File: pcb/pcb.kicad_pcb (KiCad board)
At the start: 2 copper layers, 136 x 91.9 mm, 56 parts, among them J1 BATT, J2 BATT, SW1 SW_SPST, SW10 SW_SPST, SW11 SW_SPST, SW12 SW_SPST, SW13 SW_SPST, SW14 SW_SPST, SW15 SW_SPST, SW16 SW_SPST, SW17 SW_SPST, SW18 SW_SPST, SW19 SW_SPST, SW2 SW_SPST, SW20 SW_SPST, SW21 SW_SPST, SW3 SW_SPST, SW4 SW_SPST, SW5 SW_SPST, SW6 SW_SPST, SW7 SW_SPST, SW8 SW_SPST, SW9 SW_SPST, U1 XIAO_nRF52840

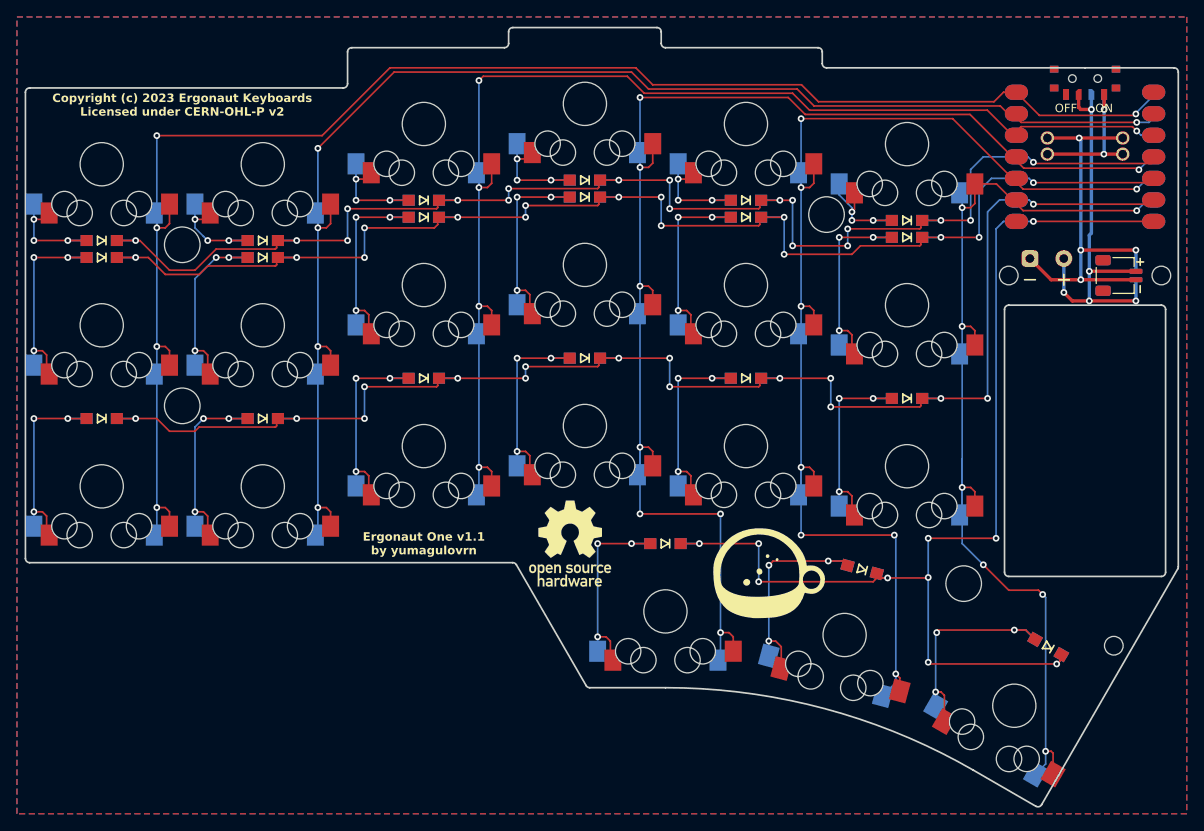
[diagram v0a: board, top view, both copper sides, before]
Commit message: fix: fix outline fillets
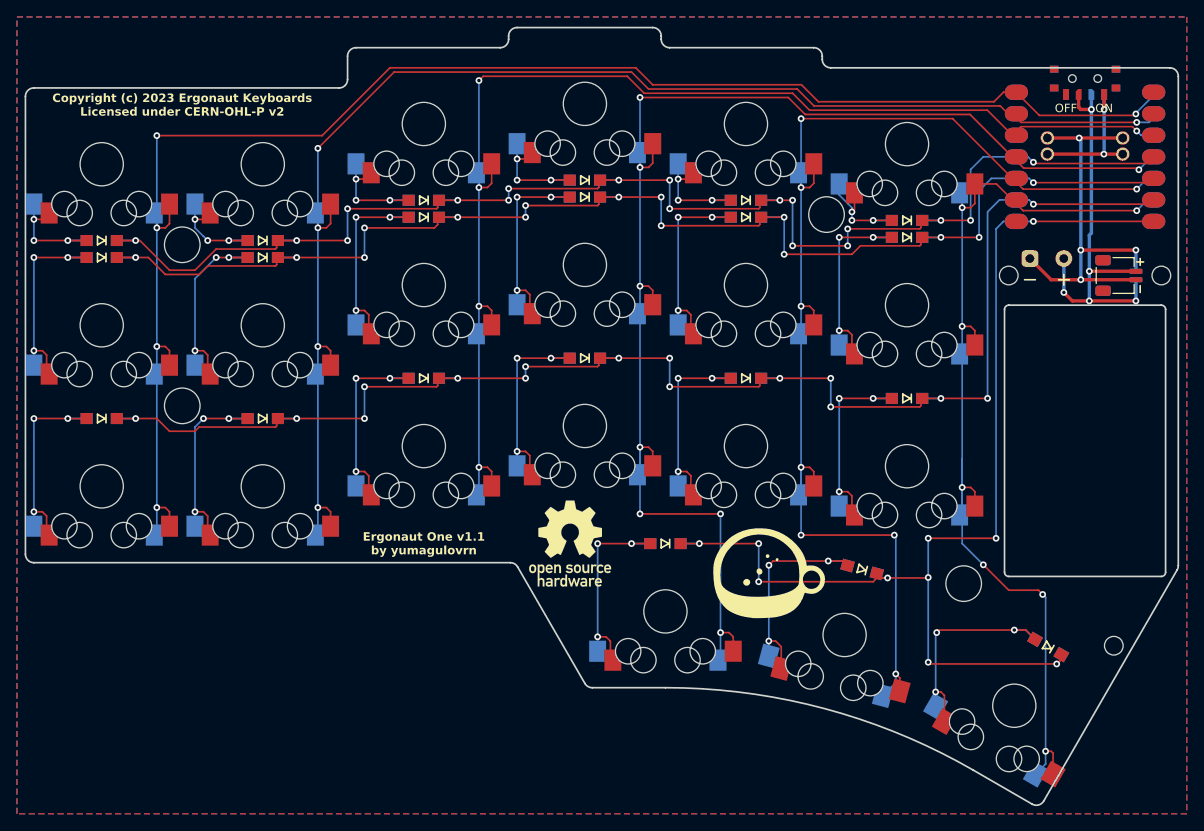
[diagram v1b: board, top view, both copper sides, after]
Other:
- board size 136 x 91.9 mm -> 136 x 91.7 mm
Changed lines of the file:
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@@
     (pad_to_mask_clearance 0)
     (aux_axis_origin 75 0)
-    (grid_origin 196.153537 0)
+    (grid_origin 75 57.49097)
     (pcbplotparams
       (layerselection 0x00010fc_ffffffff)
@@
     )
   )
-  (gr_line (start 75.5 113.49097) (end 75.5 58.49097)
+  (gr_arc (start 113.5 54.240978) (mid 113.79289 53.533866) (end 114.5 53.240978)
     (stroke (width 0.2) (type solid)) (layer "Edge.Cuts"))
-  (gr_arc (start 170 55.61597) (mid 169.646444 55.469524) (end 169.5 55.11597)
+  (gr_arc (start 210.5 55.615978) (mid 211.207104 55.908872) (end 211.5 56.615978)
     (stroke (width 0.2) (type solid)) (layer "Edge.Cuts"))
-  (gr_line (start 170 55.61597) (end 200.5 55.616046)
+  (gr_arc (start 132.695564 113.990978) (mid 133.195576 114.12494) (end 133.56159 114.490978)
     (stroke (width 0.2) (type solid)) (layer "Edge.Cuts"))
-  (gr_arc (start 142.07735 128.7407) (mid 141.827328 128.673735) (end 141.644338 128.4907)
+  (gr_line (start 132.695564 113.990978) (end 76.5 113.990978)
     (stroke (width 0.2) (type solid)) (layer "Edge.Cuts"))
-  (gr_line (start 132.5 52.74097) (end 132.5 51.36597)
+  (gr_arc (start 151 128.740708) (mid 169.805705 131.216526) (end 187.329832 138.475257)
     (stroke (width 0.2) (type solid)) (layer "Edge.Cuts"))
-  (gr_line (start 133 50.86597) (end 150 50.86597)
+  (gr_line (start 210 84.11597) (end 210 115.11597)
     (stroke (width 0.2) (type solid)) (layer "Edge.Cuts"))
-  (gr_line (start 150.5 51.36597) (end 150.5 52.74097)
+  (gr_line (start 191.5 83.61597) (end 209.5 83.61597)
     (stroke (width 0.2) (type solid)) (layer "Edge.Cuts"))
-  (gr_arc (start 211.5 114.477316) (mid 211.482974 114.60673) (end 211.433013 114.727316)
+  (gr_arc (start 132.5 51.865978) (mid 132.79289 51.158866) (end 133.5 50.865978)
     (stroke (width 0.2) (type solid)) (layer "Edge.Cuts"))
-  (gr_line (start 210 84.11597) (end 210 115.11597)
+  (gr_line (start 211.5 56.615978) (end 211.5 114.343349)
     (stroke (width 0.2) (type solid)) (layer "Edge.Cuts"))
-  (gr_line (start 211.5 56.11597) (end 211.5 114.477316)
+  (gr_line (start 151.5 53.240978) (end 168.5 53.240978)
     (stroke (width 0.2) (type solid)) (layer "Edge.Cuts"))
-  (gr_arc (start 151 53.24097) (mid 150.646444 53.094524) (end 150.5 52.74097)
+  (gr_arc (start 195.624061 142.109232) (mid 195.016852 142.575199) (end 194.258035 142.475257)
     (stroke (width 0.2) (type solid)) (layer "Edge.Cuts"))
-  (gr_line (start 191.5 83.61597) (end 209.5 83.61597)
+  (gr_line (start 141.5 128.240708) (end 133.56159 114.490978)
+    (stroke (width 0.2) (type solid)) (layer "Edge.Cuts"))
+  (gr_line (start 194.258035 142.475257) (end 187.329832 138.475257)
+    (stroke (width 0.2) (type solid)) (layer "Edge.Cuts"))
+  (gr_line (start 114.5 53.240978) (end 131.5 53.240978)
+    (stroke (width 0.2) (type solid)) (layer "Edge.Cuts"))
+  (gr_line (start 170.5 55.615978) (end 210.5 55.615978)
     (stroke (width 0.2) (type solid)) (layer "Edge.Cuts"))
-  (gr_line (start 211.433013 114.727316) (end 195.374061 142.542237)
+  (gr_arc (start 170.5 55.615978) (mid 169.79289 55.323085) (end 169.5 54.615978)
     (stroke (width 0.2) (type solid)) (layer "Edge.Cuts"))
-  (gr_arc (start 113.5 53.74097) (mid 113.646444 53.387411) (end 114 53.24097)
+  (gr_arc (start 75.5 58.990978) (mid 75.79289 58.283866) (end 76.5 57.990978)
     (stroke (width 0.2) (type solid)) (layer "Edge.Cuts"))
-  (gr_arc (start 151 128.7407) (mid 169.805705 131.216518) (end 187.329832 138.475249)
+  (gr_line (start 169.5 54.240978) (end 169.5 54.615978)
     (stroke (width 0.2) (type solid)) (layer "Edge.Cuts"))
-  (gr_arc (start 132.5 51.36597) (mid 132.646444 51.012411) (end 133 50.86597)
+  (gr_line (start 211.366025 114.843349) (end 195.624061 142.109232)
     (stroke (width 0.2) (type solid)) (layer "Edge.Cuts"))
-  (gr_arc (start 132.5 52.74097) (mid 132.353551 53.094518) (end 132 53.24097)
+  (gr_line (start 132.5 52.240978) (end 132.5 51.865978)
     (stroke (width 0.2) (type solid)) (layer "Edge.Cuts"))
-  (gr_line (start 169.5 53.74097) (end 169.5 55.11597)
+  (gr_arc (start 151.5 53.240978) (mid 150.79289 52.948085) (end 150.5 52.240978)
     (stroke (width 0.2) (type solid)) (layer "Edge.Cuts"))
   (gr_line (start 191 115.11597) (end 191 84.11597)
@@
   (gr_arc (start 210 115.11597) (mid 209.853551 115.469518) (end 209.5 115.61597)
     (stroke (width 0.2) (type solid)) (layer "Edge.Cuts"))
+  (gr_line (start 75.5 112.990978) (end 75.5 58.990978)
+    (stroke (width 0.2) (type solid)) (layer "Edge.Cuts"))
   (gr_arc (start 191.5 115.61597) (mid 191.146444 115.469524) (end 191 115.11597)
     (stroke (width 0.2) (type solid)) (layer "Edge.Cuts"))
   (gr_arc (start 191 84.11597) (mid 191.146444 83.762411) (end 191.5 83.61597)
     (stroke (width 0.2) (type solid)) (layer "Edge.Cuts"))
-  (gr_arc (start 169 53.24097) (mid 169.353551 53.387417) (end 169.5 53.74097)
-    (stroke (width 0.2) (type solid)) (layer "Edge.Cuts"))
-  (gr_arc (start 132.984239 113.99097) (mid 133.234224 114.057973) (end 133.417252 114.24097)
-    (stroke (width 0.2) (type solid)) (layer "Edge.Cuts"))
-  (gr_line (start 151 53.24097) (end 169 53.24097)
+  (gr_arc (start 142.366025 128.740708) (mid 141.866012 128.606746) (end 141.5 128.240708)
     (stroke (width 0.2) (type solid)) (layer "Edge.Cuts"))
   (gr_arc (start 209.5 83.61597) (mid 209.853551 83.762417) (end 210 84.11597)
     (stroke (width 0.2) (type solid)) (layer "Edge.Cuts"))
-  (gr_line (start 151 128.7407) (end 142.07735 128.7407)
+  (gr_line (start 133.5 50.865978) (end 149.5 50.865978)
     (stroke (width 0.2) (type solid)) (layer "Edge.Cuts"))
   (gr_line (start 209.5 115.61597) (end 191.5 115.61597)
     (stroke (width 0.2) (type solid)) (layer "Edge.Cuts"))
-  (gr_arc (start 75.5 58.49097) (mid 75.646444 58.137411) (end 76 57.99097)
-    (stroke (width 0.2) (type solid)) (layer "Edge.Cuts"))
-  (gr_line (start 114 53.24097) (end 132 53.24097)
-    (stroke (width 0.2) (type solid)) (layer "Edge.Cuts"))
-  (gr_arc (start 211 55.61597) (mid 211.353551 55.762417) (end 211.5 56.11597)
-    (stroke (width 0.2) (type solid)) (layer "Edge.Cuts"))
-  (gr_line (start 141.644338 128.4907) (end 133.417252 114.24097)
+  (gr_arc (start 113.5 56.990978) (mid 113.207104 57.69808) (end 112.5 57.990978)
     (stroke (width 0.2) (type solid)) (layer "Edge.Cuts"))
-  (gr_arc (start 76 113.99097) (mid 75.646444 113.844524) (end 75.5 113.49097)
+  (gr_arc (start 168.5 53.240978) (mid 169.207104 53.533872) (end 169.5 54.240978)
     (stroke (width 0.2) (type solid)) (layer "Edge.Cuts"))
-  (gr_line (start 132.984239 113.99097) (end 76 113.99097)
+  (gr_arc (start 149.5 50.865978) (mid 150.207104 51.158872) (end 150.5 51.865978)
     (stroke (width 0.2) (type solid)) (layer "Edge.Cuts"))
-  (gr_arc (start 150 50.86597) (mid 150.353551 51.012417) (end 150.5 51.36597)
+  (gr_arc (start 76.5 113.990978) (mid 75.792894 113.698085) (end 75.5 112.990978)
     (stroke (width 0.2) (type solid)) (layer "Edge.Cuts"))
-  (gr_line (start 194.691048 142.725249) (end 187.329832 138.475249)
+  (gr_line (start 76.5 57.990978) (end 112.5 57.990978)
     (stroke (width 0.2) (type solid)) (layer "Edge.Cuts"))
-  (gr_arc (start 113.5 57.49097) (mid 113.353551 57.844518) (end 113 57.99097)
+  (gr_line (start 151 128.740708) (end 142.366025 128.740708)
     (stroke (width 0.2) (type solid)) (layer "Edge.Cuts"))
-  (gr_line (start 113.5 57.49097) (end 113.5 53.74097)
+  (gr_arc (start 132.5 52.240978) (mid 132.207104 52.94808) (end 131.5 53.240978)
     (stroke (width 0.2) (type solid)) (layer "Edge.Cuts"))
-  (gr_line (start 76 57.99097) (end 113 57.99097)
+  (gr_line (start 150.5 51.865978) (end 150.5 52.240978)
     (stroke (width 0.2) (type solid)) (layer "Edge.Cuts"))
-  (gr_line (start 200.5 55.616046) (end 211 55.61597)
+  (gr_line (start 113.5 56.990978) (end 113.5 54.240978)
     (stroke (width 0.2) (type solid)) (layer "Edge.Cuts"))
-  (gr_arc (start 195.374061 142.542237) (mid 195.070453 142.775244) (end 194.691048 142.725249)
+  (gr_arc (start 211.5 114.343349) (mid 211.465931 114.60217) (end 211.366025 114.843349)
     (stroke (width 0.2) (type solid)) (layer "Edge.Cuts"))
   (gr_circle (center 172.135076 122.523186) (end 173.135076 122.523186)
